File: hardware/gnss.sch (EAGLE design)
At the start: 39 parts, among them J1 MICRO_USB_B_HIROSE_ZX62-B-5PA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, SW1 TVAF06-A020B-R, U2 NJM12888F, X1 FA-238

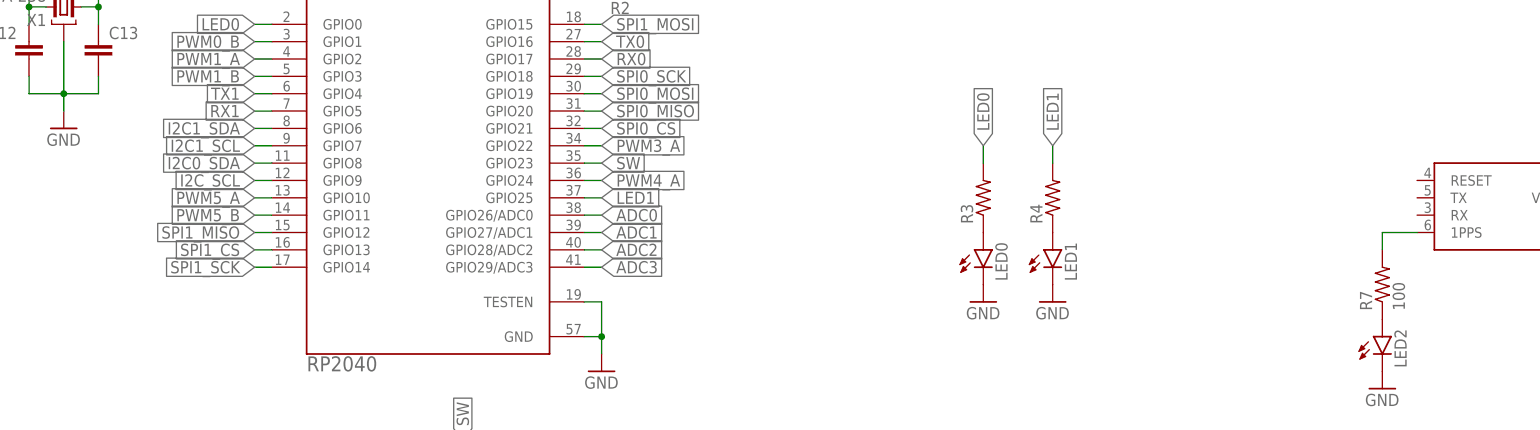
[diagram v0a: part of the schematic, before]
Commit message: 変更点: communication_LoRaをUART接続に変換 gnss_GPSのRTX接続およびRESETの追加
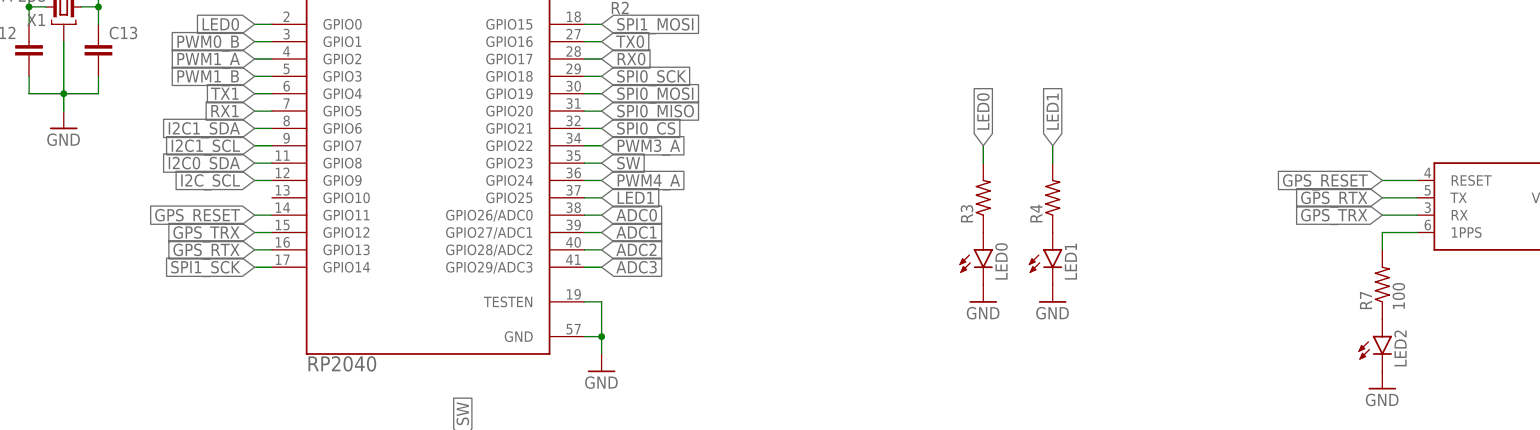
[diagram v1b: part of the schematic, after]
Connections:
- removed net PWM5_A: RP1.GPIO10
- removed net PWM5_B: RP1.GPIO11
- removed net SPI1_CS: RP1.GPIO13
- removed net SPI1_MISO: RP1.GPIO12
- new net GPS_RESET: RP1.GPIO11, U$1.RESET
- new net GPS_RTX: RP1.GPIO13, U$1.TX
- new net GPS_TRX: RP1.GPIO12, U$1.RX
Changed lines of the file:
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@@
-</segment>
-</net>
-<net name="SPI1_CS" class="0">
-<segment>
-<pinref part="RP1" gate="G$1" pin="GPIO13"/>
-<wire x1="33.02" y1="63.5" x2="30.48" y2="63.5" width="0.1524" layer="91"/>
-<label x="30.48" y="63.5" size="1.778" layer="95" rot="R180" xref="yes"/>
-</segment>
-</net>
-<net name="SPI1_MISO" class="0">
-<segment>
-<pinref part="RP1" gate="G$1" pin="GPIO12"/>
-<wire x1="33.02" y1="66.04" x2="30.48" y2="66.04" width="0.1524" layer="91"/>
-<label x="30.48" y="66.04" size="1.778" layer="95" rot="R180" xref="yes"/>
 </segment>
 </net>
@@
 <wire x1="78.74" y1="73.66" x2="81.28" y2="73.66" width="0.1524" layer="91"/>
 <label x="81.28" y="73.66" size="1.778" layer="95" xref="yes"/>
-</segment>
-</net>
-<net name="PWM5_A" class="0">
-<segment>
-<pinref part="RP1" gate="G$1" pin="GPIO10"/>
-<wire x1="33.02" y1="71.12" x2="30.48" y2="71.12" width="0.1524" layer="91"/>
-<label x="30.48" y="71.12" size="1.778" layer="95" rot="R180" xref="yes"/>
-</segment>
-</net>
-<net name="PWM5_B" class="0">
-<segment>
-<pinref part="RP1" gate="G$1" pin="GPIO11"/>
-<wire x1="33.02" y1="68.58" x2="30.48" y2="68.58" width="0.1524" layer="91"/>
-<label x="30.48" y="68.58" size="1.778" layer="95" rot="R180" xref="yes"/>
 </segment>
 </net>
@@
 </segment>
 </net>
+<net name="GPS_RESET" class="0">
+<segment>
+<pinref part="U$1" gate="G$1" pin="RESET"/>
+<wire x1="200.66" y1="73.66" x2="195.58" y2="73.66" width="0.1524" layer="91"/>
+<label x="195.58" y="73.66" size="1.778" layer="95" rot="R180" xref="yes"/>
+</segment>
+<segment>
+<pinref part="RP1" gate="G$1" pin="GPIO11"/>
+<wire x1="33.02" y1="68.58" x2="30.48" y2="68.58" width="0.1524" layer="91"/>
+<label x="30.48" y="68.58" size="1.778" layer="95" rot="R180" xref="yes"/>
+</segment>
+</net>
+<net name="GPS_RTX" class="0">
+<segment>
+<pinref part="U$1" gate="G$1" pin="TX"/>
+<wire x1="200.66" y1="71.12" x2="195.58" y2="71.12" width="0.1524" layer="91"/>
+<label x="195.58" y="71.12" size="1.778" layer="95" rot="R180" xref="yes"/>
+</segment>
+<segment>
+<pinref part="RP1" gate="G$1" pin="GPIO13"/>
+<wire x1="33.02" y1="63.5" x2="30.48" y2="63.5" width="0.1524" layer="91"/>
+<label x="30.48" y="63.5" size="1.778" layer="95" rot="R180" xref="yes"/>
+</segment>
+</net>
+<net name="GPS_TRX" class="0">
+<segment>
+<pinref part="U$1" gate="G$1" pin="RX"/>
+<wire x1="200.66" y1="68.58" x2="195.58" y2="68.58" width="0.1524" layer="91"/>
+<label x="195.58" y="68.58" size="1.778" layer="95" rot="R180" xref="yes"/>
+</segment>
+<segment>
+<pinref part="RP1" gate="G$1" pin="GPIO12"/>
+<wire x1="33.02" y1="66.04" x2="30.48" y2="66.04" width="0.1524" layer="91"/>
+<label x="30.48" y="66.04" size="1.778" layer="95" rot="R180" xref="yes"/>
+</segment>
+</net>

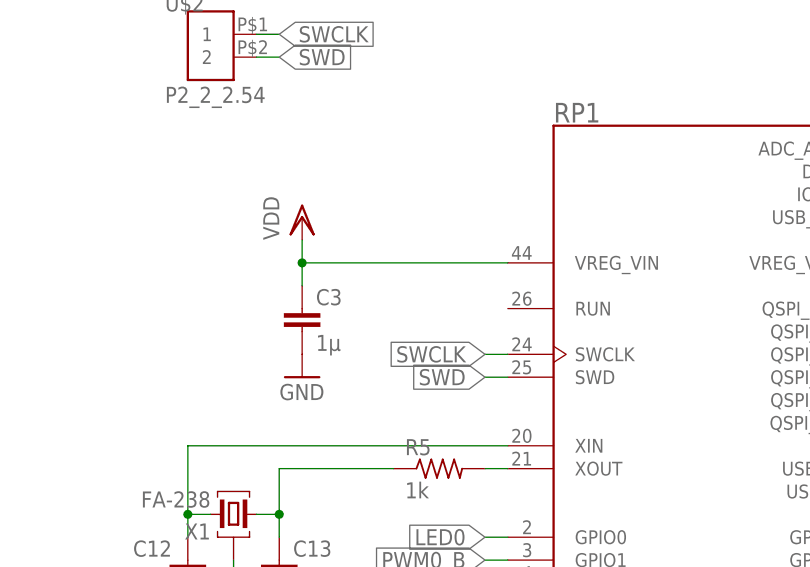
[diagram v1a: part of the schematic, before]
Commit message: べたGND前です。esp32のschはノータッチなのでここに上がってないです。よろしくお願いします。
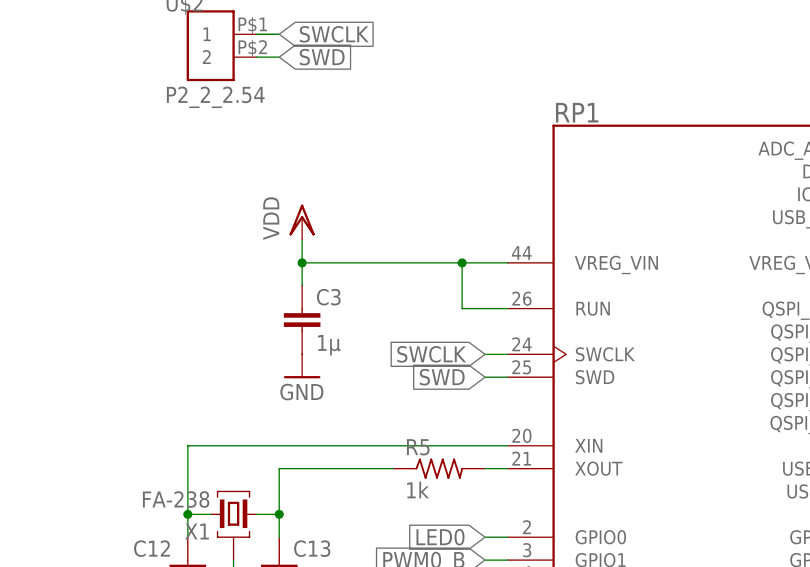
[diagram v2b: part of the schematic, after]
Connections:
- net VDD: now also RP1.RUN
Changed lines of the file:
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@@
 <segment>
 <pinref part="RP1" gate="G$1" pin="VREG_VIN"/>
-<wire x1="33.02" y1="127" x2="10.16" y2="127" width="0.1524" layer="91"/>
+<wire x1="33.02" y1="127" x2="27.94" y2="127" width="0.1524" layer="91"/>
 <pinref part="C3" gate="G$1" pin="1"/>
+<wire x1="27.94" y1="127" x2="10.16" y2="127" width="0.1524" layer="91"/>
 <wire x1="10.16" y1="127" x2="10.16" y2="124.46" width="0.1524" layer="91"/>
 <wire x1="10.16" y1="127" x2="10.16" y2="129.54" width="0.1524" layer="91"/>
 <junction x="10.16" y="127"/>
 <pinref part="VDD8" gate="G$1" pin="VDD"/>
+<pinref part="RP1" gate="G$1" pin="RUN"/>
+<wire x1="33.02" y1="121.92" x2="27.94" y2="121.92" width="0.1524" layer="91"/>
+<wire x1="27.94" y1="121.92" x2="27.94" y2="127" width="0.1524" layer="91"/>
+<junction x="27.94" y="127"/>
 </segment>
 <segment>

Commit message: シルクを調整
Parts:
- renumbered BT1 to BAT, U$1 to GNSS
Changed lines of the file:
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@@
 <part name="BOTTOM" library="pins" deviceset="P5_2.54" device=""/>
 <part name="U$2" library="pins" deviceset="P2_2_2.54" device=""/>
-<part name="U$1" library="gps" deviceset="GYSFDMAXB" device=""/>
+<part name="GNSS" library="gps" deviceset="GYSFDMAXB" device=""/>
 <part name="D2" library="diodes" deviceset="CUHS20S30" device=""/>
 <part name="VDD1" library="supply1" library_urn="urn:adsk.eagle:library:371" deviceset="VDD" device=""/>
@@
 <part name="GND4" library="supply1" library_urn="urn:adsk.eagle:library:371" deviceset="GND" device=""/>
 <part name="GND5" library="supply1" library_urn="urn:adsk.eagle:library:371" deviceset="GND" device=""/>
-<part name="BT1" library="MS414GE-FL26E" deviceset="MS414GE-FL26E" device=""/>
+<part name="BAT" library="MS414GE-FL26E" deviceset="MS414GE-FL26E" device=""/>
 </parts>
 <sheets>
@@
 <attribute name="VALUE" x="-5.08" y="144.78" size="1.778" layer="96"/>
 </instance>
-<instance part="U$1" gate="G$1" x="218.44" y="68.58" smashed="yes" rot="MR0">
+<instance part="GNSS" gate="G$1" x="218.44" y="68.58" smashed="yes" rot="MR0">
 <attribute name="VALUE" x="233.68" y="60.96" size="1.27" layer="96" rot="MR0"/>
 </instance>
@@
 <attribute name="VALUE" x="243.84" y="71.12" size="1.778" layer="96"/>
 </instance>
-<instance part="BT1" gate="G$1" x="259.08" y="60.96" smashed="yes" rot="R270">
+<instance part="BAT" gate="G$1" x="259.08" y="60.96" smashed="yes" rot="R270">
 <attribute name="NAME" x="262.89" y="64.77" size="1.778" layer="95" rot="R270"/>
 <attribute name="VALUE" x="269.24" y="64.77" size="1.778" layer="96" rot="R270"/>
@@
 </segment>
 <segment>
-<pinref part="U$1" gate="G$1" pin="GND"/>
+<pinref part="GNSS" gate="G$1" pin="GND"/>
 <wire x1="238.76" y1="66.04" x2="241.3" y2="66.04" width="0.1524" layer="91"/>
 <wire x1="241.3" y1="66.04" x2="241.3" y2="60.96" width="0.1524" layer="91"/>
@@
 <segment>
 <pinref part="GND2" gate="1" pin="GND"/>
-<pinref part="BT1" gate="G$1" pin="-"/>
+<pinref part="BAT" gate="G$1" pin="-"/>
 </segment>
 </net>
@@
 </segment>
 <segment>
-<pinref part="U$1" gate="G$1" pin="VDD3V3"/>
+<pinref part="GNSS" gate="G$1" pin="VDD3V3"/>
 <wire x1="238.76" y1="73.66" x2="241.3" y2="73.66" width="0.1524" layer="91"/>
 <wire x1="241.3" y1="73.66" x2="241.3" y2="86.36" width="0.1524" layer="91"/>
@@
 <net name="N$1" class="0">
 <segment>
-<pinref part="U$1" gate="G$1" pin="VDD3V3_BACKUP"/>
+<pinref part="GNSS" gate="G$1" pin="VDD3V3_BACKUP"/>
 <wire x1="238.76" y1="71.12" x2="251.46" y2="71.12" width="0.1524" layer="91"/>
 <wire x1="251.46" y1="71.12" x2="259.08" y2="71.12" width="0.1524" layer="91"/>
@@
 <wire x1="251.46" y1="68.58" x2="251.46" y2="71.12" width="0.1524" layer="91"/>
 <junction x="251.46" y="71.12"/>
-<pinref part="BT1" gate="G$1" pin="+"/>
+<pinref part="BAT" gate="G$1" pin="+"/>
 </segment>
 </net>
@@
 <net name="N$3" class="0">
 <segment>
-<pinref part="U$1" gate="G$1" pin="1PPS"/>
+<pinref part="GNSS" gate="G$1" pin="1PPS"/>
 <wire x1="200.66" y1="66.04" x2="195.58" y2="66.04" width="0.1524" layer="91"/>
 <wire x1="195.58" y1="66.04" x2="195.58" y2="63.5" width="0.1524" layer="91"/>
@@
 <net name="GPS_RESET" class="0">
 <segment>
-<pinref part="U$1" gate="G$1" pin="RESET"/>
+<pinref part="GNSS" gate="G$1" pin="RESET"/>
 <wire x1="200.66" y1="73.66" x2="195.58" y2="73.66" width="0.1524" layer="91"/>
 <label x="195.58" y="73.66" size="1.778" layer="95" rot="R180" xref="yes"/>
@@
 <net name="GPS_RTX" class="0">
 <segment>
-<pinref part="U$1" gate="G$1" pin="TX"/>
+<pinref part="GNSS" gate="G$1" pin="TX"/>
 <wire x1="200.66" y1="71.12" x2="195.58" y2="71.12" width="0.1524" layer="91"/>
 <label x="195.58" y="71.12" size="1.778" layer="95" rot="R180" xref="yes"/>
@@
 <net name="GPS_TRX" class="0">
 <segment>
-<pinref part="U$1" gate="G$1" pin="RX"/>
+<pinref part="GNSS" gate="G$1" pin="RX"/>
 <wire x1="200.66" y1="68.58" x2="195.58" y2="68.58" width="0.1524" layer="91"/>
 <label x="195.58" y="68.58" size="1.778" layer="95" rot="R180" xref="yes"/>
